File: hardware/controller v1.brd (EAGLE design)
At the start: 71.1 x 73.9 mm, 35 parts, among them CON1 1X08-CONN3.5MM, CON2 1X08-CONN3.5MM, CON3 1X08-CONN3.5MM, CON4 1X08-CONN3.5MM, IC1 MC33880PEG, IC2 L293DD, IC3 MC33880PEG

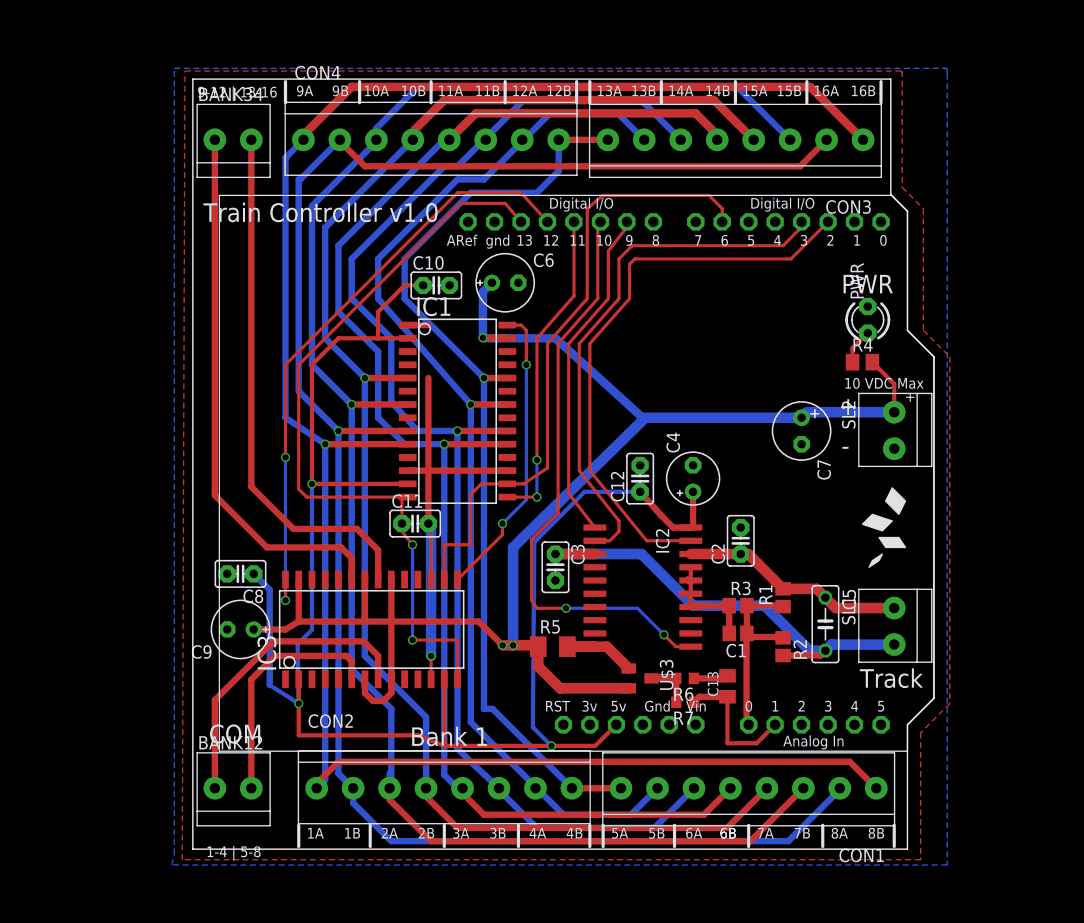
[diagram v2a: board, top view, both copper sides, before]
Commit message: Update on board layout for Arduino shield.
Better layout, added component names.
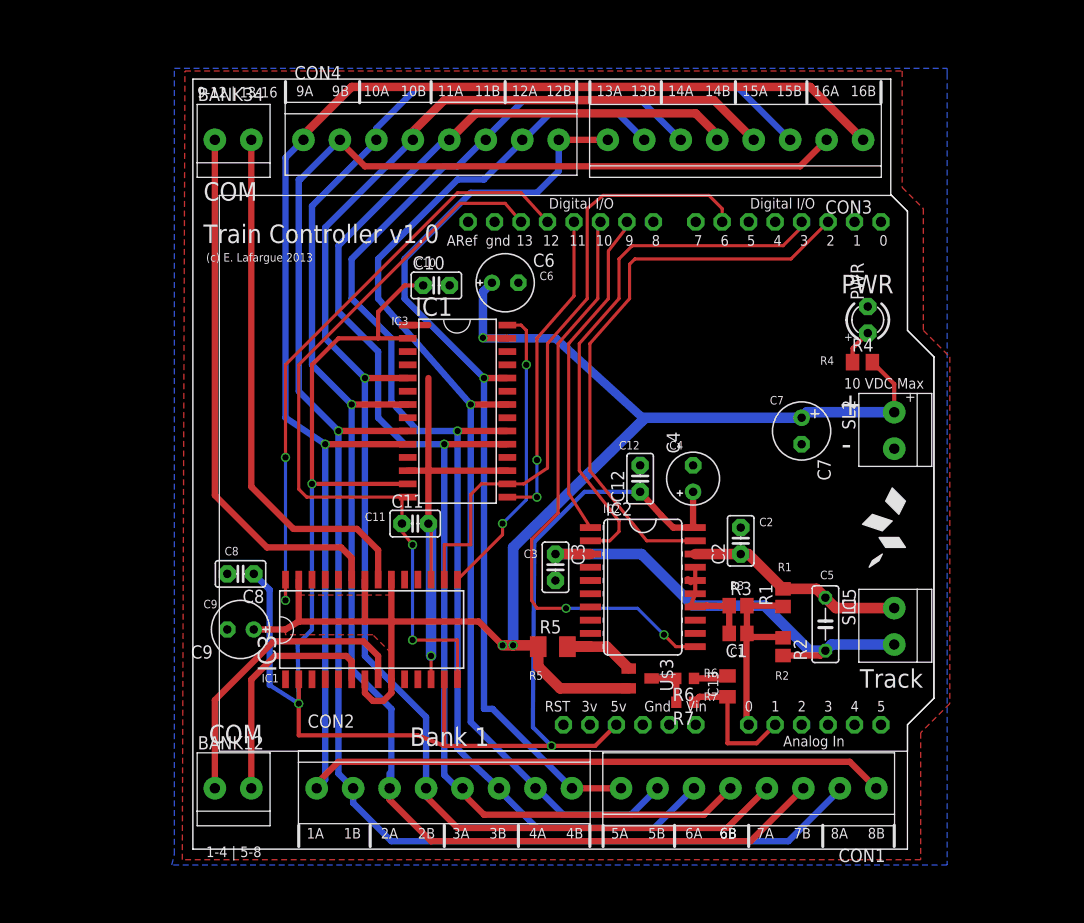
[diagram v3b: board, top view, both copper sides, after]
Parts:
- C11: value 0.1uF 6V -> 1pF 6V
- IC2: device l293dd:SO20 -> aerodynes:SOIC20-2
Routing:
- added copper zone on layer 1, net V+
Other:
- board text added: "(c) E. Lafargue 2013"
- board text added: "C1"
- board text added: "C10"
- board text added: "C11"
- board text added: "C12"
- board text added: "C2"
- board text added: "C3"
- board text added: "C4"
- board text added: "C5"
- board text added: "C6"
- board text added: "C7"
- board text added: "C8"
- board text added: "C9"
- board text added: "IC1"
- board text added: "IC2"
- board text added: "IC3"
- board text added: "R1"
- board text added: "R2"
- board text added: "R3"
- board text added: "R4"
- board text added: "R5"
- board text added: "R6"
- board text added: "R7"
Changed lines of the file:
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@@
 <layer number="49" name="Reference" color="7" fill="1" visible="yes" active="yes"/>
 <layer number="50" name="dxf" color="7" fill="1" visible="no" active="yes"/>
-<layer number="51" name="tDocu" color="7" fill="1" visible="yes" active="yes"/>
+<layer number="51" name="tDocu" color="7" fill="1" visible="no" active="yes"/>
 <layer number="52" name="bDocu" color="7" fill="1" visible="yes" active="yes"/>
 <layer number="53" name="tGND_GNDA" color="7" fill="9" visible="no" active="no"/>
@@
 <text x="78.994" y="44.704" size="1.016" layer="21">10 VDC Max</text>
 <text x="84.836" y="43.434" size="1.016" layer="21">+</text>
-<text x="78.486" y="42.164" size="1.778" layer="21">+</text>
-<text x="78.74" y="38.354" size="1.778" layer="21">-</text>
+<text x="78.486" y="42.164" size="2.1844" layer="21">+</text>
+<text x="78.74" y="38.354" size="2.1844" layer="21">-</text>
 <text x="24.638" y="73.66" size="1.016" layer="21" rot="R180">9-12 | 13-16</text>
 <text x="37.338" y="10.414" size="1.778" layer="21">Bank 1</text>
 <text x="18.034" y="10.668" size="1.778" layer="21">COM</text>
-<text x="17.526" y="60.706" size="1.778" layer="21">Train Controller v1.0</text>
+<text x="17.526" y="58.674" size="1.778" layer="21">Train Controller v1.0</text>
 <text x="78.74" y="53.848" size="1.778" layer="21">PWR</text>
 <text x="80.518" y="16.002" size="1.778" layer="21">Track</text>
@@
 <text x="76.073" y="72.771" size="1.016" layer="21">16A</text>
 <text x="79.629" y="72.771" size="1.016" layer="21">16B</text>
+<text x="23.114" y="16.51" size="0.8128" layer="21">IC1</text>
+<text x="55.88" y="32.766" size="0.8128" layer="21">IC2</text>
+<text x="35.56" y="50.8" size="0.8128" layer="21">IC3</text>
+<text x="33.02" y="32.004" size="0.8128" layer="21">C11</text>
+<text x="37.846" y="56.388" size="0.8128" layer="21">C10</text>
+<text x="49.784" y="55.118" size="0.8128" layer="21">C6</text>
+<text x="19.558" y="28.702" size="0.8128" layer="21">C8</text>
+<text x="17.526" y="23.622" size="0.8128" layer="21">C9</text>
+<text x="48.768" y="16.764" size="0.8128" layer="21">R5</text>
+<text x="65.532" y="17.018" size="0.8128" layer="21">R6</text>
+<text x="68.072" y="25.4" size="0.8128" layer="21">R3</text>
+<text x="68.072" y="19.05" size="0.8128" layer="21">C1</text>
+<text x="76.708" y="26.416" size="0.8128" layer="21">C5</text>
+<text x="70.866" y="31.496" size="0.8128" layer="21">C2</text>
+<text x="48.26" y="28.448" size="0.8128" layer="21">C3</text>
+<text x="76.708" y="46.99" size="0.8128" layer="21">R4</text>
+<text x="71.882" y="43.18" size="0.8128" layer="21">C7</text>
+<text x="57.404" y="38.862" size="0.8128" layer="21">C12</text>
+<text x="62.23" y="38.862" size="0.8128" layer="21">C4</text>
+<text x="78.994" y="49.276" size="0.8128" layer="21">+</text>
+<text x="65.532" y="14.732" size="0.8128" layer="21">R7</text>
+<text x="72.39" y="16.764" size="0.8128" layer="21">R2</text>
+<text x="72.644" y="27.178" size="0.8128" layer="21">R1</text>
+<text x="17.526" y="62.738" size="1.778" layer="21">COM</text>
+<text x="17.78" y="56.896" size="0.8128" layer="21">(c) E. Lafargue 2013</text>
 </plain>
 <attributes>
@@
 </autorouter>
 <elements>
-<element name="IC2" library="l293dd" package="SO20" value="L293DD" x="59.69" y="25.654" rot="R270"/>
+<element name="IC2" library="aerodynes" package="SOIC20-2" value="L293DD" x="59.69" y="25.654" rot="R270"/>
 <element name="SL1" library="adafruit" package="1X2-3.5MM" value="1X2-3.5MM" x="83.82" y="21.844" rot="R90"/>
 <element name="U$1" library="aerodynes" package="ARDUINO-NOCUT" value="ARDUINO" x="30.48" y="45.466"/>
@@
 <element name="C9" library="rcl" package="E2,5-6E" value="10uF 20V" x="21.082" y="21.59" rot="R180"/>
 <element name="C10" library="rcl-ez" package="C025-025X050" value="0.1uF 6V" x="39.878" y="54.61"/>
-<element name="C11" library="rcl-ez" package="C025-025X050" value="0.1uF 6V" x="37.846" y="31.75"/>
+<element name="C11" library="rcl-ez" package="C025-025X050" value="1pF 6V" x="37.846" y="31.75"/>
 <element name="BANK12" library="adafruit" package="1X2-3.5MM" value="1X2-3.5MM" x="20.32" y="6.35"/>
 <element name="BANK34" library="adafruit" package="1X2-3.5MM" value="1X2-3.5MM" x="20.32" y="68.58"/>
@@
 <wire x1="39.116" y1="31.75" x2="39.116" y2="36.83" width="0.6096" layer="1"/>
 <contactref element="C3" pad="2"/>
-<wire x1="64.29" y1="27.559" x2="64.29" y2="26.289" width="0.4064" layer="1"/>
-<wire x1="64.29" y1="26.289" x2="64.29" y2="25.019" width="0.4064" layer="1"/>
-<wire x1="64.29" y1="25.019" x2="64.29" y2="23.876" width="0.4064" layer="1"/>
+<wire x1="64.7192" y1="27.559" x2="64.7192" y2="26.289" width="0.4064" layer="1"/>
+<wire x1="64.7192" y1="26.289" x2="64.7192" y2="25.019" width="0.4064" layer="1"/>
+<wire x1="64.7192" y1="25.019" x2="64.29" y2="23.876" width="0.4064" layer="1"/>
 <wire x1="67.984" y1="23.876" x2="67.984" y2="21.209" width="0.6096" layer="1"/>
-<wire x1="64.29" y1="23.749" x2="64.29" y2="23.876" width="0.6096" layer="1"/>
+<wire x1="64.7192" y1="23.749" x2="64.29" y2="23.876" width="0.6096" layer="1"/>
 <wire x1="64.29" y1="26.134" x2="64.008" y2="26.416" width="0.6096" layer="1"/>
 <wire x1="67.984" y1="23.876" x2="67.095" y2="23.837" width="0.6096" layer="1"/>
@@
 <wire x1="26.565903125" y1="20.19091875" x2="26.565903125" y2="20.170096875" width="0.4064" layer="16"/>
 <wire x1="26.565903125" y1="20.170096875" x2="26.67" y2="14.478" width="0.4064" layer="16"/>
-<wire x1="64.29" y1="31.369" x2="62.611" y2="31.369" width="0.6096" layer="1"/>
+<wire x1="64.7192" y1="31.369" x2="62.611" y2="31.369" width="0.6096" layer="1"/>
 <wire x1="62.611" y1="31.369" x2="61.468" y2="32.512" width="0.6096" layer="1"/>
 <contactref element="C12" pad="1"/>
 <wire x1="59.436" y1="34.798" x2="61.468" y2="32.512" width="0.6096" layer="1"/>
 <wire x1="64.516" y1="34.798" x2="64.516" y2="31.595" width="0.6096" layer="1"/>
-<wire x1="64.516" y1="31.595" x2="64.29" y2="31.369" width="0.6096" layer="1"/>
+<wire x1="64.516" y1="31.595" x2="64.7192" y2="31.369" width="0.6096" layer="1"/>
 <via x="50.927" y="10.414" extent="1-16" drill="0.6" shape="square"/>
 <wire x1="50.927" y1="10.414" x2="49.149" y2="12.192" width="0.4064" layer="16"/>
@@
 <wire x1="73.152" y1="19.089" x2="76.747" y2="19.089" width="0.6096" layer="1"/>
 <wire x1="76.747" y1="19.089" x2="77.216" y2="19.558" width="0.6096" layer="1"/>
-<wire x1="55.09" y1="28.829" x2="51.308" y2="28.829" width="1.016" layer="1"/>
+<wire x1="54.6608" y1="28.829" x2="51.308" y2="28.829" width="1.016" layer="1"/>
 </signal>
 <signal name="V+">
@@
 <wire x1="34.798" y1="14.732" x2="35.56" y2="15.494" width="0.6096" layer="1"/>
 <wire x1="35.56" y1="15.494" x2="35.56" y2="16.81" width="0.6096" layer="1"/>
+<polygon width="0" layer="1">
+<vertex x="25.4" y="21.844"/>
+<vertex x="26.67" y="22.606"/>
+<vertex x="26.67" y="24.892"/>
+<vertex x="35.56" y="24.892"/>
+<vertex x="35.56" y="19.304"/>
+<vertex x="33.782" y="21.082"/>
+<vertex x="25.4" y="21.082"/>
+</polygon>
 </signal>
 <signal name="PWM1">
@@
 <wire x1="56.388" y1="53.34" x2="52.578" y2="49.022" width="0.3048" layer="1"/>
 <wire x1="52.578" y1="49.022" x2="52.578" y2="34.643" width="0.3048" layer="1"/>
-<wire x1="52.578" y1="34.643" x2="55.09" y2="31.369" width="0.3048" layer="1"/>
+<wire x1="52.578" y1="34.643" x2="54.6608" y2="31.369" width="0.3048" layer="1"/>
 </signal>
 <signal name="PWM2">
@@
 <via x="61.722" y="21.082" extent="1-16" drill="0.6" shape="square"/>
 <wire x1="61.722" y1="21.082" x2="62.865" y2="19.939" width="0.3048" layer="1"/>
-<wire x1="62.865" y1="19.939" x2="64.29" y2="19.939" width="0.3048" layer="1"/>
+<wire x1="62.865" y1="19.939" x2="64.7192" y2="19.939" width="0.3048" layer="1"/>
 <wire x1="55.372" y1="60.706" x2="55.626" y2="60.706" width="0.3048" layer="1"/>
 </signal>
@@
 <wire x1="83.82" y1="23.644" x2="78.21" y2="23.644" width="1.016" layer="1"/>
 <wire x1="78.21" y1="23.644" x2="77.216" y2="24.638" width="1.016" layer="1"/>
-<wire x1="69.088" y1="28.829" x2="64.29" y2="28.829" width="1.016" layer="1"/>
+<wire x1="69.088" y1="28.829" x2="64.7192" y2="28.829" width="1.016" layer="1"/>
 <wire x1="69.088" y1="28.829" x2="69.811" y2="28.829" width="1.016" layer="1"/>
 <wire x1="69.811" y1="28.829" x2="73.152" y2="25.488" width="1.016" layer="1"/>
@@
 <signal name="1A">
 <contactref element="IC2" pad="2"/>
-<wire x1="55.09" y1="30.099" x2="56.515" y2="30.099" width="0.3048" layer="1"/>
+<wire x1="54.6608" y1="30.099" x2="56.515" y2="30.099" width="0.3048" layer="1"/>
 <wire x1="56.515" y1="30.099" x2="57.404" y2="30.988" width="0.3048" layer="1"/>
 <wire x1="57.404" y1="30.988" x2="57.404" y2="32.004" width="0.3048" layer="1"/>
@@
 <wire x1="54.61" y1="49.022" x2="54.61" y2="36.83" width="0.3048" layer="1"/>
 <wire x1="54.61" y1="36.83" x2="60.071" y2="30.099" width="0.3048" layer="1"/>
-<wire x1="60.071" y1="30.099" x2="64.29" y2="30.099" width="0.3048" layer="1"/>
+<wire x1="60.071" y1="30.099" x2="64.7192" y2="30.099" width="0.3048" layer="1"/>
 </signal>
 <signal name="BEMF_MEASURE">
@@
 <contactref element="R5" pad="2"/>
 <contactref element="IC2" pad="10"/>
-<wire x1="52.454" y1="19.939" x2="55.09" y2="19.939" width="1.016" layer="1"/>
+<wire x1="52.454" y1="19.939" x2="54.6608" y2="19.939" width="1.016" layer="1"/>
 <contactref element="U$3" pad="3"/>
 <wire x1="52.454" y1="19.939" x2="56.238" y2="19.939" width="1.016" layer="1"/>

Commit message: Diagnostics screen works now!
Complete board diagnostics, including port open circuit detection.
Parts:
- C11: device rcl-ez:C025-025X050 -> rcl-ez:C0805K
- moved C11 0.25 mm to (38.1, 31.8)
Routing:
- net GND: track 60.8 -> 34.7 mm, vias 1 -> 19
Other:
- board text added: "C13"
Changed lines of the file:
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@@
 <text x="55.88" y="32.766" size="0.8128" layer="21">IC2</text>
 <text x="35.56" y="50.8" size="0.8128" layer="21">IC3</text>
-<text x="33.02" y="32.004" size="0.8128" layer="21">C11</text>
+<text x="34.036" y="31.242" size="0.8128" layer="21">C11</text>
 <text x="37.846" y="56.388" size="0.8128" layer="21">C10</text>
 <text x="49.784" y="55.118" size="0.8128" layer="21">C6</text>
@@
 <text x="17.526" y="62.738" size="1.778" layer="21">COM</text>
 <text x="17.78" y="56.896" size="0.8128" layer="21">(c) E. Lafargue 2013</text>
+<text x="69.088" y="16.002" size="0.8128" layer="21">C13</text>
 </plain>
 <attributes>
@@
 <element name="C9" library="rcl" package="E2,5-6E" value="10uF 20V" x="21.082" y="21.59" rot="R180"/>
 <element name="C10" library="rcl-ez" package="C025-025X050" value="0.1uF 6V" x="39.878" y="54.61"/>
-<element name="C11" library="rcl-ez" package="C025-025X050" value="1pF 6V" x="37.846" y="31.75"/>
+<element name="C11" library="rcl-ez" package="C0805K" value="1pF 6V" x="38.1" y="31.75"/>
 <element name="BANK12" library="adafruit" package="1X2-3.5MM" value="1X2-3.5MM" x="20.32" y="6.35"/>
 <element name="BANK34" library="adafruit" package="1X2-3.5MM" value="1X2-3.5MM" x="20.32" y="68.58"/>
@@
 <contactref element="C11" pad="2"/>
 <wire x1="37.13" y1="50.8" x2="39.116" y2="50.8" width="0.6096" layer="1"/>
-<wire x1="39.116" y1="45.72" x2="39.116" y2="36.83" width="0.6096" layer="1"/>
-<wire x1="39.116" y1="36.83" x2="37.13" y2="36.83" width="0.6096" layer="1"/>
-<wire x1="46.69" y1="36.83" x2="39.116" y2="36.83" width="0.6096" layer="1"/>
-<wire x1="39.116" y1="31.75" x2="39.116" y2="36.83" width="0.6096" layer="1"/>
 <contactref element="C3" pad="2"/>
 <wire x1="64.7192" y1="27.559" x2="64.7192" y2="26.289" width="0.4064" layer="1"/>
@@
 <contactref element="IC3" pad="17"/>
 <contactref element="IC3" pad="12"/>
-<wire x1="39.37" y1="26.37" x2="39.37" y2="31.496" width="0.3048" layer="1"/>
-<wire x1="39.37" y1="31.496" x2="39.116" y2="31.75" width="0.3048" layer="1"/>
+<wire x1="39.37" y1="26.37" x2="39.37" y2="29.718" width="0.3048" layer="1"/>
+<wire x1="39.37" y1="29.718" x2="39.37" y2="31.496" width="0.3048" layer="1"/>
+<wire x1="39.37" y1="31.496" x2="39.1" y2="31.75" width="0.3048" layer="1"/>
 <wire x1="39.37" y1="16.81" x2="39.37" y2="19.05" width="0.3048" layer="1"/>
 <via x="39.37" y="19.05" extent="1-16" drill="0.6" shape="square"/>
-<wire x1="39.37" y1="19.05" x2="39.37" y2="31.496" width="1.016" layer="16"/>
-<wire x1="39.37" y1="31.496" x2="39.243" y2="31.623" width="0.3048" layer="16"/>
-<wire x1="39.243" y1="31.623" x2="39.243" y2="31.877" width="0.3048" layer="16"/>
-<wire x1="39.243" y1="31.877" x2="39.116" y2="32.004" width="0.3048" layer="16"/>
-<wire x1="39.116" y1="32.004" x2="39.116" y2="31.75" width="0.3048" layer="16"/>
-<polygon width="0.3048" layer="1" isolate="0.3048" thermals="no">
+<wire x1="39.37" y1="19.05" x2="39.37" y2="29.718" width="1.016" layer="16"/>
+<polygon width="0.3048" layer="1" isolate="0.3048" thermals="no" rank="2">
 <vertex x="15.748" y="75.184"/>
 <vertex x="84.582" y="75.184"/>
@@
 <contactref element="PWR" pad="K"/>
 <contactref element="SL2" pad="2"/>
-<polygon width="0.254" layer="16" isolate="0.3048">
+<polygon width="0.254" layer="16" isolate="0.3048" rank="2">
 <vertex x="14.732" y="0"/>
 <vertex x="14.732" y="75.438"/>
@@
 <contactref element="IC1" pad="4"/>
 <contactref element="IC1" pad="3"/>
+<via x="39.37" y="29.718" extent="1-16" drill="0.6" shape="square"/>
+<via x="20.32" y="37.084" extent="1-16" drill="0.6" shape="square"/>
+<via x="35.052" y="37.592" extent="1-16" drill="0.6" shape="square"/>
+<via x="69.342" y="38.354" extent="1-16" drill="0.6" shape="square"/>
+<via x="74.93" y="29.21" extent="1-16" drill="0.6" shape="square"/>
+<via x="46.99" y="16.256" extent="1-16" drill="0.6" shape="square"/>
+<via x="59.69" y="25.654" extent="1-16" drill="0.6" shape="square"/>
+<via x="74.93" y="32.766" extent="1-16" drill="0.6" shape="square"/>
+<via x="74.93" y="36.068" extent="1-16" drill="0.6" shape="square"/>
+<via x="69.342" y="36.068" extent="1-16" drill="0.6" shape="square"/>
+<via x="80.264" y="64.008" extent="1-16" drill="0.6" shape="square"/>
+<via x="69.596" y="64.008" extent="1-16" drill="0.6" shape="square"/>
+<via x="53.848" y="64.008" extent="1-16" drill="0.6" shape="square"/>
+<via x="42.926" y="57.404" extent="1-16" drill="0.6" shape="square"/>
+<via x="51.562" y="57.404" extent="1-16" drill="0.6" shape="square"/>
+<via x="20.32" y="49.784" extent="1-16" drill="0.6" shape="square"/>
+<via x="25.4" y="8.382" extent="1-16" drill="0.6" shape="square"/>
+<via x="76.2" y="16.002" extent="1-16" drill="0.6" shape="square"/>
 </signal>
 <signal name="VCC">
@@
 <wire x1="27.432" y1="34.29" x2="36.576" y2="34.29" width="0.3048" layer="1"/>
 <wire x1="36.576" y1="34.29" x2="37.13" y2="34.29" width="0.3048" layer="1"/>
-<wire x1="36.576" y1="31.75" x2="36.576" y2="34.29" width="0.3048" layer="1"/>
-<wire x1="36.576" y1="31.75" x2="36.576" y2="30.988" width="0.3048" layer="1"/>
-<wire x1="36.576" y1="30.988" x2="37.592" y2="29.718" width="0.3048" layer="1"/>
+<wire x1="37.1" y1="31.75" x2="36.576" y2="34.29" width="0.3048" layer="1"/>
+<wire x1="37.1" y1="31.75" x2="37.592" y2="30.988" width="0.3048" layer="1"/>
+<wire x1="37.592" y1="30.988" x2="37.592" y2="29.718" width="0.3048" layer="1"/>
 <wire x1="41.91" y1="16.81" x2="41.91" y2="20.574" width="0.3048" layer="1"/>
 <wire x1="41.91" y1="20.574" x2="37.592" y2="20.574" width="0.3048" layer="1"/>
